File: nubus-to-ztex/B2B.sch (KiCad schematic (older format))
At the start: 17 parts, among them J1 Conn_02x07_Odd_Even, J3 Conn_01x06_Male

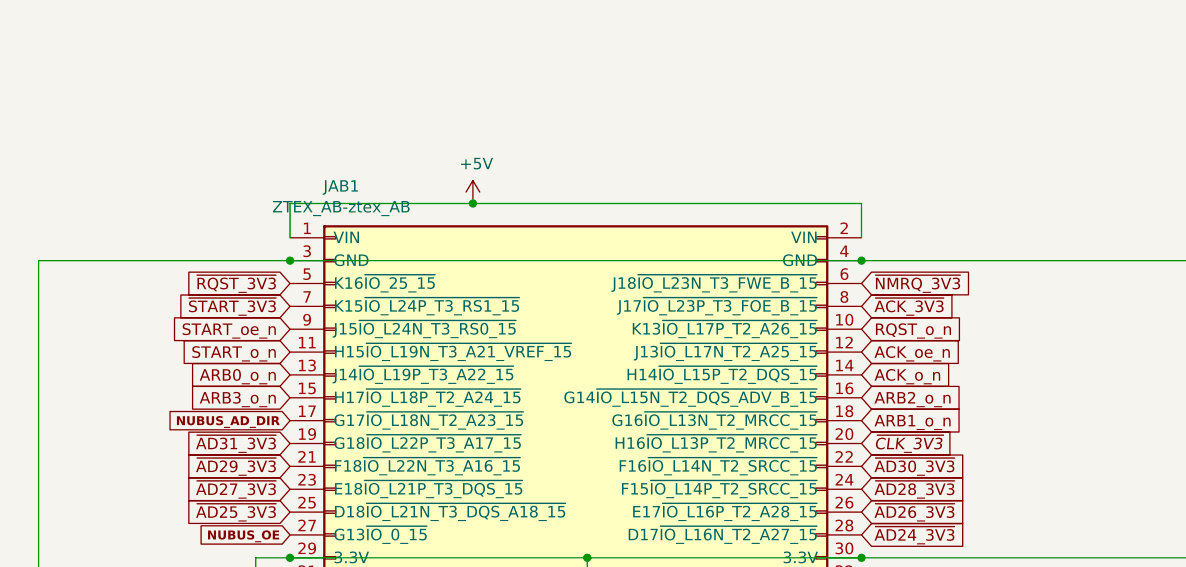
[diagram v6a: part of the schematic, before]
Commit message: reinstate some useful debug LEDs
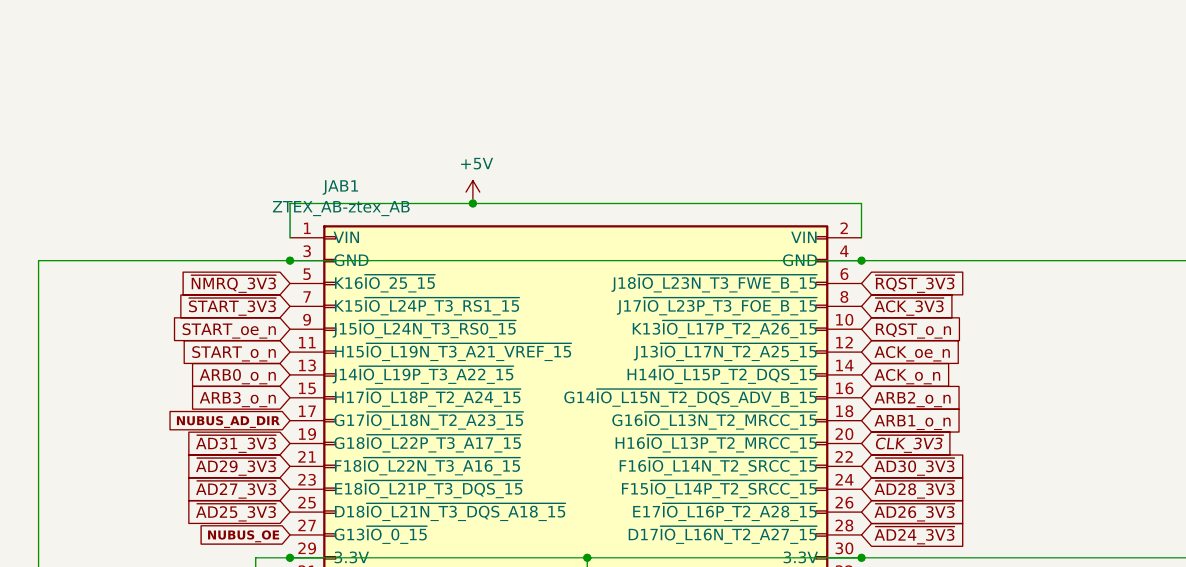
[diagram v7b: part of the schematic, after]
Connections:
- net ~NMRQ_3V3: now also JAB1.5 (K16~IO_25_15); no longer JAB1.6 (J18~IO_L23N_T3_FWE_B_15)
- net ~RQST_3V3: now also JAB1.6 (J18~IO_L23N_T3_FWE_B_15); no longer JAB1.5 (K16~IO_25_15)
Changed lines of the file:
@@
 Text GLabel 4100 2050 2    50   Input Italic 0
 ~CLK_3V3
-Text GLabel 1600 1350 0    50   Input ~ 0
+Text GLabel 4100 1350 2    50   Input ~ 0
 ~RQST_3V3
 Text GLabel 1600 1450 0    50   Input ~ 0
@@
 Text Notes 1200 5650 0    50   ~ 0
 User LEDS
-Text GLabel 4100 1350 2    50   Input ~ 0
+Text GLabel 1600 1350 0    50   Input ~ 0
 ~NMRQ_3V3
 Text GLabel 9900 3550 2    50   Input ~ 0

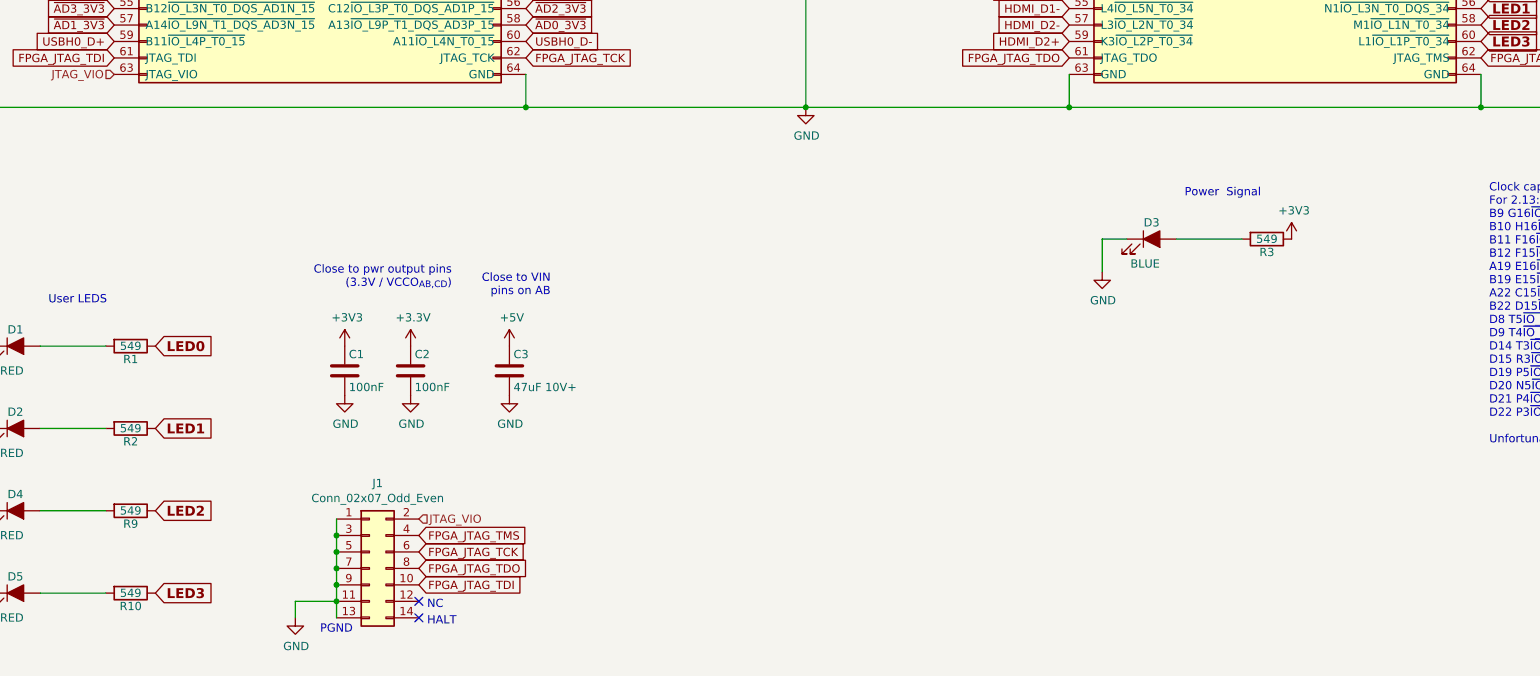
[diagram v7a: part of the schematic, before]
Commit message: cut down brightness of LEDs, more 2x32 pin headers reference
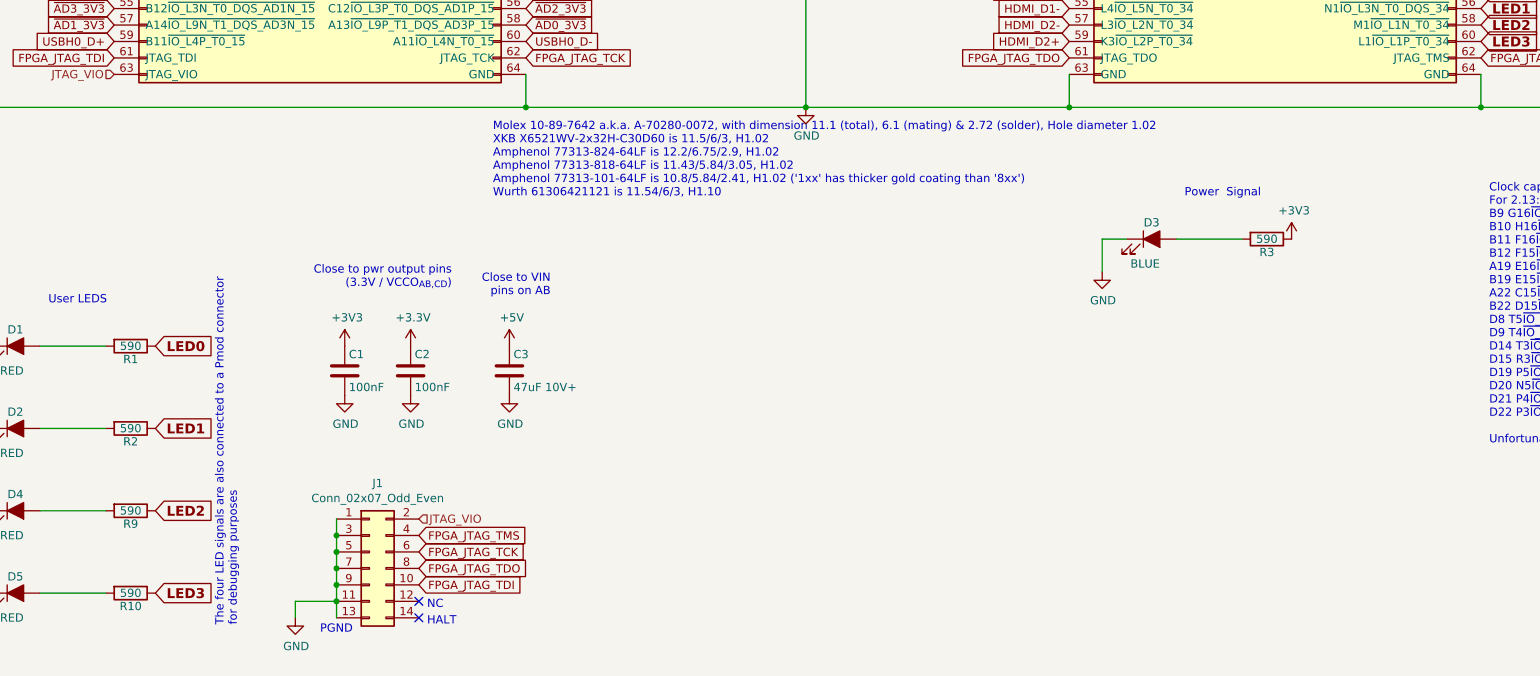
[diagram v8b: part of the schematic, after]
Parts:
- JAB1, JCD1: MPN X6521WV-2x32H-C30D60 -> 77313-101-64LF; MPN (Molex) (none) -> 10-89-7642; MPN (XKB) (none) -> X6521WV-2x32H-C30D60; MPN-ALT 10-89-7642 -> (none); URL https://www2.mouser.com/ProductDetail/Molex/10-89-7642?qs=%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 -> https://eu.mouser.com/ProductDetail/Amphenol-FCI/77313-101-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; URL (Molex) (none) -> https://www2.mouser.com/ProductDetail/Molex/10-89-7642?qs=%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; URL (XKB) (none) -> https://www.lcsc.com/product-detail/Pin-Headers_XKB-Connect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
- R1, R10, R2, R3, R9: value 549 -> 590; MPN 0603WAF5490T5E -> 0603WAF5900T5E; URL https://lcsc.com/product-detail/Chip-Resistor-Surface-Mount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 -> https://www.lcsc.com/product-detail/Chip-Resistor-Surface-M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
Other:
- note added: "Molex 10-89-7642 a.k.a. A-70280-0072, with dimension 11.1 (total), 6.1 (mating) & 2.72 (solder), Hole diameter 1.02\nXKB X6521WV-2x32H-C30D60 is 11.5/6/3, H1.02\nAmphenol 77313-824-64LF is 12.2/6.75/2.9, H1.02\nAmphenol 77313-818-64LF is 11.43/5.84/3.05, H1.02\nAmphenol 77313-101-64LF is 10.8/5.84/2.41, H1.02 ('1xx' has thicker gold coating than '8xx')\nWurth 61306421121 is 11.54/6/3, H1.10\n"
- note added: "The four LED signals are also connected to a Pmod connector\nfor debugging purposes"
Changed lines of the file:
@@
 $Descr A4 11693 8268
 encoding utf-8
-Sheet 2 9
+Sheet 2 10
 Title "nubus-to-ztex B2B connector"
 Date ""
@@
 F 2 "For_SeeedStudio:PinHeader_2x32_P2.54mm_Vertical_For_SeeedStudio" H 1800 2650 50  0001 C CNN
 F 3 "" H 1800 2650 50  0001 C CNN
-F 4 "10-89-7642" H 1800 2650 50  0001 C CNN "MPN-ALT"
-F 5 "https://www2.mouser.com/ProductDetail/Molex/10-89-7642?qs=%2Fha2pyFadugCxzQFZUdvioDcljDVidgd4vXrOFuSRYM%3D" H 1800 2650 50  0001 C CNN "URL"
-F 6 "X6521WV-2x32H-C30D60" H 1800 2650 50  0001 C CNN "MPN"
+F 4 "10-89-7642" H 1800 2650 50  0001 C CNN "MPN (Molex)"
+F 5 "https://www2.mouser.com/ProductDetail/Molex/10-89-7642?qs=%2Fha2pyFadugCxzQFZUdvioDcljDVidgd4vXrOFuSRYM%3D" H 1800 2650 50  0001 C CNN "URL (Molex)"
+F 6 "X6521WV-2x32H-C30D60" H 1800 2650 50  0001 C CNN "MPN (XKB)"
+F 7 "https://www.lcsc.com/product-detail/Pin-Headers_XKB-Connectivity-X6521WV-2x32H-C30D60_C2883966.html" H 1800 2650 50  0001 C CNN "URL (XKB)"
+F 8 "77313-101-64LF" H 1800 2650 50  0001 C CNN "MPN"
+F 9 "https://eu.mouser.com/ProductDetail/Amphenol-FCI/77313-101-64LF?qs=xJiur%252Bgubk1MSan%2F7C0v%252BA%3D%3D" H 1800 2650 50  0001 C CNN "URL"
 	1    1800 2650
 	1    0    0    -1
@@
 F 2 "For_SeeedStudio:PinHeader_2x32_P2.54mm_Vertical_For_SeeedStudio" H 7600 2650 50  0001 C CNN
 F 3 "" H 7600 2650 50  0001 C CNN
-F 4 "10-89-7642" H 7600 2650 50  0001 C CNN "MPN-ALT"
-F 5 "https://www2.mouser.com/ProductDetail/Molex/10-89-7642?qs=%2Fha2pyFadugCxzQFZUdvioDcljDVidgd4vXrOFuSRYM%3D" H 7600 2650 50  0001 C CNN "URL"
-F 6 "X6521WV-2x32H-C30D60" H 7600 2650 50  0001 C CNN "MPN"
+F 4 "10-89-7642" H 1800 2650 50  0001 C CNN "MPN (Molex)"
+F 5 "https://www2.mouser.com/ProductDetail/Molex/10-89-7642?qs=%2Fha2pyFadugCxzQFZUdvioDcljDVidgd4vXrOFuSRYM%3D" H 1800 2650 50  0001 C CNN "URL (Molex)"
+F 6 "X6521WV-2x32H-C30D60" H 1800 2650 50  0001 C CNN "MPN (XKB)"
+F 7 "https://www.lcsc.com/product-detail/Pin-Headers_XKB-Connectivity-X6521WV-2x32H-C30D60_C2883966.html" H 1800 2650 50  0001 C CNN "URL (XKB)"
+F 8 "77313-101-64LF" H 1800 2650 50  0001 C CNN "MPN"
+F 9 "https://eu.mouser.com/ProductDetail/Amphenol-FCI/77313-101-64LF?qs=xJiur%252Bgubk1MSan%2F7C0v%252BA%3D%3D" H 1800 2650 50  0001 C CNN "URL"
 	1    7600 2650
 	1    0    0    -1
@@
 AR Path="/618E8C75/61B5DFBC" Ref="R1"  Part="1"
 F 0 "R1" V 1780 5900 50  0000 C CNN
-F 1 "549" V 1700 5900 50  0000 C CNN
+F 1 "590" V 1700 5900 50  0000 C CNN
 F 2 "Resistor_SMD:R_0603_1608Metric" V 1630 5900 50  0001 C CNN
 F 3 "" H 1700 5900 50  0000 C CNN
-F 4 "0603WAF5490T5E" V 1700 5900 50  0001 C CNN "MPN"
-F 5 "https://lcsc.com/product-detail/Chip-Resistor-Surface-Mount_UNI-ROYAL-Uniroyal-Elec-0603WAF5490T5E_C23079.html" V 1700 5900 50  0001 C CNN "URL"
+F 4 "0603WAF5900T5E" V 1700 5900 50  0001 C CNN "MPN"
+F 5 "https://www.lcsc.com/product-detail/Chip-Resistor-Surface-Mount_UNI-ROYAL-Uniroyal-Elec-0603WAF5900T5E_C23084.html" V 1700 5900 50  0001 C CNN "URL"
 	1    1700 5900
 	0    1    1    0
@@
 AR Path="/618E8C75/61B5F3F5" Ref="R2"  Part="1"
 F 0 "R2" V 1780 6400 50  0000 C CNN
-F 1 "549" V 1700 6400 50  0000 C CNN
+F 1 "590" V 1700 6400 50  0000 C CNN
 F 2 "Resistor_SMD:R_0603_1608Metric" V 1630 6400 50  0001 C CNN
 F 3 "" H 1700 6400 50  0000 C CNN
-F 4 "0603WAF5490T5E" V 1700 6400 50  0001 C CNN "MPN"
-F 5 "https://lcsc.com/product-detail/Chip-Resistor-Surface-Mount_UNI-ROYAL-Uniroyal-Elec-0603WAF5490T5E_C23079.html" V 1700 6400 50  0001 C CNN "URL"
+F 4 "0603WAF5900T5E" V 1700 6400 50  0001 C CNN "MPN"
+F 5 "https://www.lcsc.com/product-detail/Chip-Resistor-Surface-Mount_UNI-ROYAL-Uniroyal-Elec-0603WAF5900T5E_C23084.html" V 1700 6400 50  0001 C CNN "URL"
 	1    1700 6400
 	0    1    1    0
@@
 AR Path="/618E8C75/621E3C4D" Ref="R3"  Part="1"
 F 0 "R3" V 8680 5250 50  0000 C CNN
-F 1 "549" V 8600 5250 50  0000 C CNN
+F 1 "590" V 8600 5250 50  0000 C CNN
 F 2 "Resistor_SMD:R_0603_1608Metric" V 8530 5250 50  0001 C CNN
 F 3 "" H 8600 5250 50  0000 C CNN
-F 4 "0603WAF5490T5E" V 8600 5250 50  0001 C CNN "MPN"
-F 5 "https://lcsc.com/product-detail/Chip-Resistor-Surface-Mount_UNI-ROYAL-Uniroyal-Elec-0603WAF5490T5E_C23079.html" V 8600 5250 50  0001 C CNN "URL"
+F 4 "0603WAF5900T5E" V 8600 5250 50  0001 C CNN "MPN"
+F 5 "https://www.lcsc.com/product-detail/Chip-Resistor-Surface-Mount_UNI-ROYAL-Uniroyal-Elec-0603WAF5900T5E_C23084.html" V 8600 5250 50  0001 C CNN "URL"
 	1    8600 5250
 	0    1    1    0
@@
 AR Path="/618E8C75/62CD698B" Ref="R9"  Part="1"
 F 0 "R9" V 1780 6900 50  0000 C CNN
-F 1 "549" V 1700 6900 50  0000 C CNN
+F 1 "590" V 1700 6900 50  0000 C CNN
 F 2 "Resistor_SMD:R_0603_1608Metric" V 1630 6900 50  0001 C CNN
 F 3 "" H 1700 6900 50  0000 C CNN
-F 4 "0603WAF5490T5E" V 1700 6900 50  0001 C CNN "MPN"
-F 5 "https://lcsc.com/product-detail/Chip-Resistor-Surface-Mount_UNI-ROYAL-Uniroyal-Elec-0603WAF5490T5E_C23079.html" V 1700 6900 50  0001 C CNN "URL"
+F 4 "0603WAF5900T5E" V 1700 6900 50  0001 C CNN "MPN"
+F 5 "https://www.lcsc.com/product-detail/Chip-Resistor-Surface-Mount_UNI-ROYAL-Uniroyal-Elec-0603WAF5900T5E_C23084.html" V 1700 6900 50  0001 C CNN "URL"
 	1    1700 6900
 	0    1    1    0
@@
 AR Path="/618E8C75/62CD69A8" Ref="R10"  Part="1"
 F 0 "R10" V 1780 7400 50  0000 C CNN
-F 1 "549" V 1700 7400 50  0000 C CNN
+F 1 "590" V 1700 7400 50  0000 C CNN
 F 2 "Resistor_SMD:R_0603_1608Metric" V 1630 7400 50  0001 C CNN
 F 3 "" H 1700 7400 50  0000 C CNN
-F 4 "0603WAF5490T5E" V 1700 7400 50  0001 C CNN "MPN"
-F 5 "https://lcsc.com/product-detail/Chip-Resistor-Surface-Mount_UNI-ROYAL-Uniroyal-Elec-0603WAF5490T5E_C23079.html" V 1700 7400 50  0001 C CNN "URL"
+F 4 "0603WAF5900T5E" V 1700 7400 50  0001 C CNN "MPN"
+F 5 "https://www.lcsc.com/product-detail/Chip-Resistor-Surface-Mount_UNI-ROYAL-Uniroyal-Elec-0603WAF5900T5E_C23084.html" V 1700 7400 50  0001 C CNN "URL"
 	1    1700 7400
 	0    1    1    0
@@
 Text GLabel 9900 4050 2    60   Input ~ 12
 LED3
+Text Notes 3900 5000 0    50   ~ 0
+Molex 10-89-7642 a.k.a. A-70280-0072, with dimension 11.1 (total), 6.1 (mating) & 2.72 (solder), Hole diameter 1.02\nXKB X6521WV-2x32H-C30D60 is 11.5/6/3, H1.02\nAmphenol 77313-824-64LF is 12.2/6.75/2.9, H1.02\nAmphenol 77313-818-64LF is 11.43/5.84/3.05, H1.02\nAmphenol 77313-101-64LF is 10.8/5.84/2.41, H1.02 ('1xx' has thicker gold coating than '8xx')\nWurth 61306421121 is 11.54/6/3, H1.10\n
+Text Notes 2350 7600 1    50   ~ 0
+The four LED signals are also connected to a Pmod connector\nfor debugging purposes
 $EndSCHEMATC
